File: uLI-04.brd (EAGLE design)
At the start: 57 x 38.5 mm, 39 parts, among them IC1 PIC18F14K50-I/SS, IC2 ADM2483, IC4 78L05F, J1 PICPROG2-V, J5 WEBP6-4, J6 WEBP6-4, J7 WEBP6-4, Q1 12.00 MHz, T1 IRF7306, X1 MINI-USB_SHIELD4P-USB-SPEC, X2 ARK1550/2_S

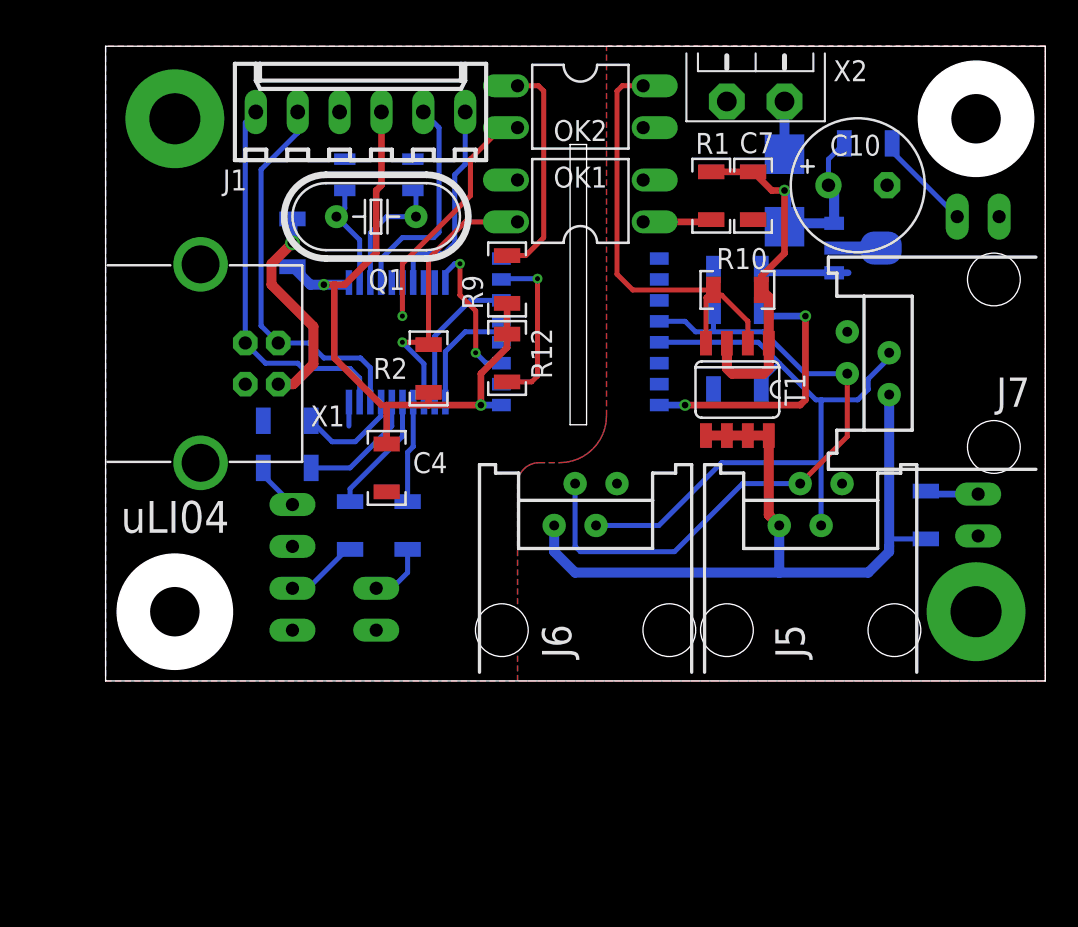
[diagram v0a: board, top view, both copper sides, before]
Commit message: uLI-04 rev 2.
Opraveny chyby uLI-04 zjistene behem testovani:
 * upraven obrys krabicky podle realnych rozmeru (zvetseno symtetricky 1 mm do sirky a 0.5 mm do vysky)
 * posunuty otvory pro srouby do krabicky o 0.5 mm v kazde ose smerrem ke kraji
 * prohozeno RX a TX mezi procesorem a ADUMem
 * opraveno zdcadlove zapojeni XpressNETich konektoru
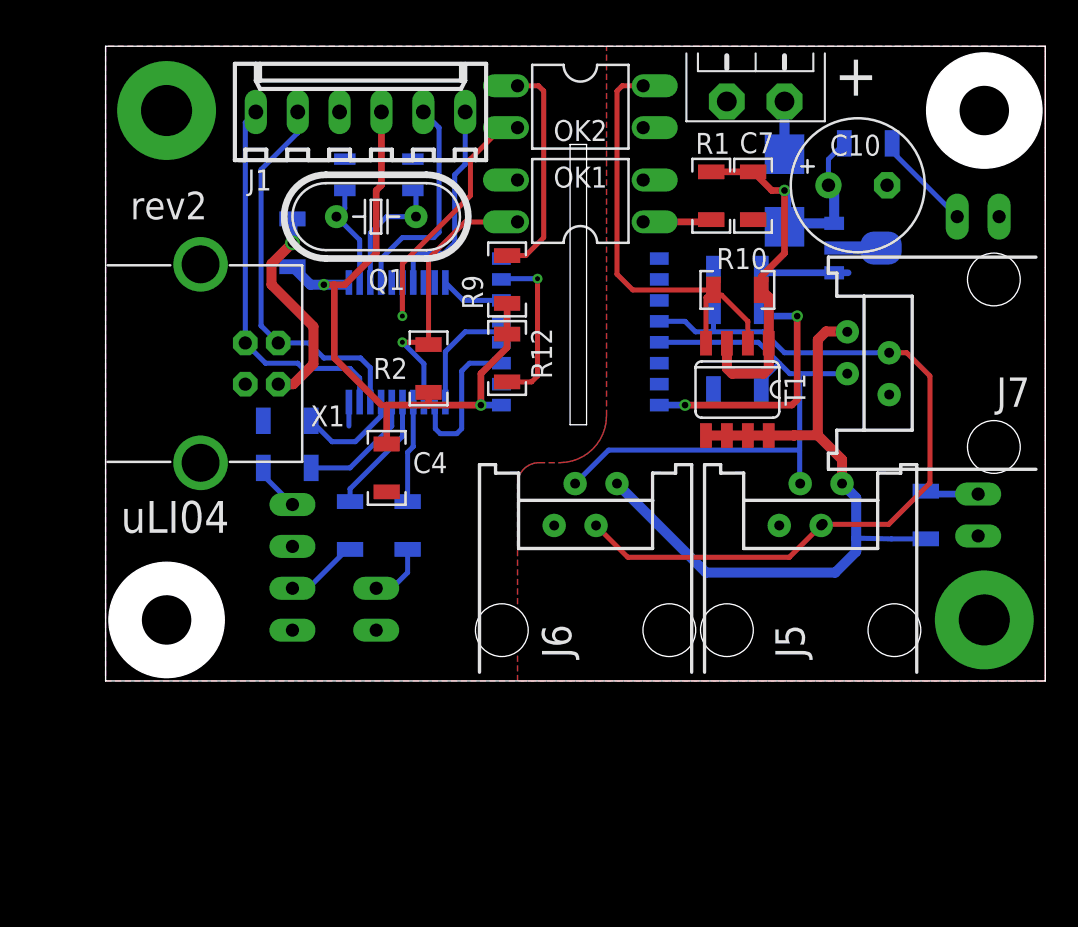
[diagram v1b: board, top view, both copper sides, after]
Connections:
- removed net PROC_TX: IC1.10, IC2.3
- new net N$5: IC1.12, IC2.3
- net +NAP: now also J5.4, J6.4, J7.4; no longer J5.1, J6.1, J7.1
- net BUS_A: now also J5.3, J6.3, J7.3; no longer J5.2, J6.2, J7.2
- net BUS_B: now also J5.2, J6.2, J7.2; no longer J5.3, J6.3, J7.3
- net GNDINT: now also J5.1, J6.1, J7.1; no longer J5.4, J6.4, J7.4
- net PROC_RX: now also IC1.10; no longer IC1.12
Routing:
- net N$5: track 0.00 -> 9.59 mm
- net PROC_TX: track 9.31 -> 0.00 mm, vias 2 -> 0
- net BUS_A: track 41.2 -> 48.7 mm, vias 0 -> 1
- net BUS_B: track 42.0 -> 35.4 mm
- net PROC_RX: track 8.94 -> 3.85 mm
- net +NAP: track 47.4 -> 44.1 mm
- net VCCINT: track 24.8 -> 23.8 mm
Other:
- outline, holes or cut-outs redrawn
- board text added: "+"
- board text added: "rev2"

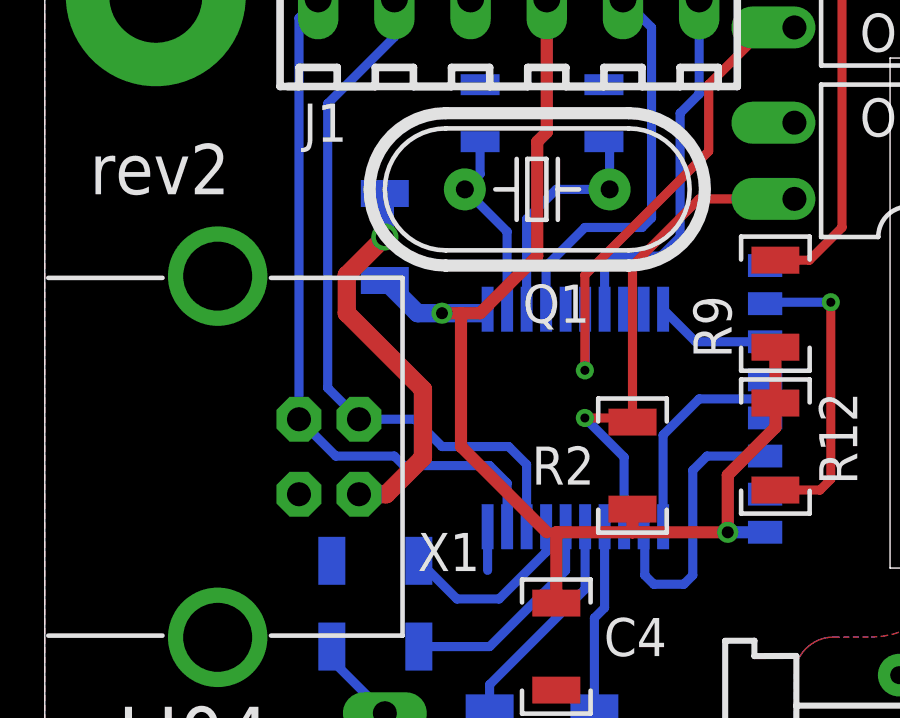
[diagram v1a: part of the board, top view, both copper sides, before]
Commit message: Odstranena ochrana dioda na vstupu z USB.
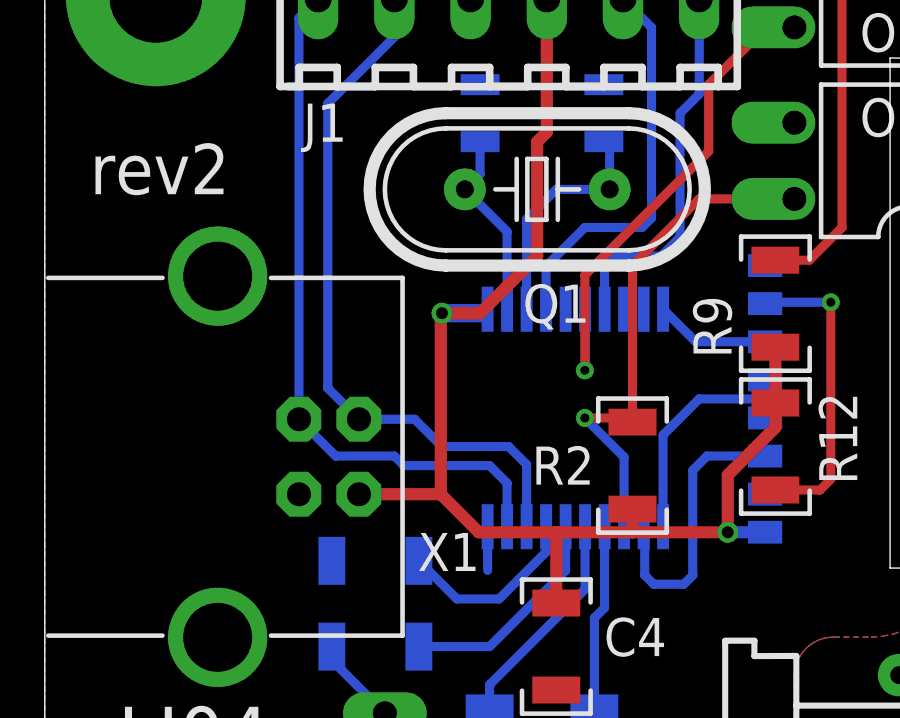
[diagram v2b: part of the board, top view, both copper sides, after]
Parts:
- removed D1: 1N4148-1206, diode:D1206
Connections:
- removed net N$10: D1.A, X1.1
- net VDD: now also X1.1; no longer D1.C
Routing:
- net N$10: track 13.0 -> 0.00 mm, vias 1 -> 0
- net VDD: track 42.3 -> 44.3 mm
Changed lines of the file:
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@@
 <layer number="14" name="Route14" color="1" fill="6" visible="no" active="no"/>
 <layer number="15" name="Route15" color="4" fill="6" visible="no" active="no"/>
-<layer number="16" name="Bottom" color="4" fill="1" visible="no" active="yes"/>
+<layer number="16" name="Bottom" color="4" fill="1" visible="yes" active="yes"/>
 <layer number="17" name="Pads" color="2" fill="1" visible="yes" active="yes"/>
 <layer number="18" name="Vias" color="2" fill="1" visible="yes" active="yes"/>
@@
 <layer number="20" name="Dimension" color="15" fill="1" visible="yes" active="yes"/>
 <layer number="21" name="tPlace" color="7" fill="1" visible="yes" active="yes"/>
-<layer number="22" name="bPlace" color="7" fill="1" visible="no" active="yes"/>
+<layer number="22" name="bPlace" color="7" fill="1" visible="yes" active="yes"/>
 <layer number="23" name="tOrigins" color="15" fill="1" visible="yes" active="yes"/>
-<layer number="24" name="bOrigins" color="15" fill="1" visible="no" active="yes"/>
-<layer number="25" name="tNames" color="7" fill="1" visible="yes" active="yes"/>
+<layer number="24" name="bOrigins" color="15" fill="1" visible="yes" active="yes"/>
+<layer number="25" name="tNames" color="7" fill="1" visible="no" active="yes"/>
 <layer number="26" name="bNames" color="7" fill="1" visible="no" active="yes"/>
 <layer number="27" name="tValues" color="7" fill="1" visible="no" active="yes"/>
@@
 <layer number="44" name="Drills" color="7" fill="1" visible="no" active="yes"/>
 <layer number="45" name="Holes" color="7" fill="1" visible="no" active="yes"/>
-<layer number="46" name="Milling" color="3" fill="1" visible="no" active="yes"/>
+<layer number="46" name="Milling" color="3" fill="1" visible="yes" active="yes"/>
 <layer number="47" name="Measures" color="7" fill="1" visible="no" active="yes"/>
 <layer number="48" name="Document" color="7" fill="1" visible="no" active="yes"/>
-<layer number="49" name="Reference" color="7" fill="1" visible="no" active="yes"/>
+<layer number="49" name="Reference" color="7" fill="1" visible="yes" active="yes"/>
 <layer number="50" name="dxf" color="7" fill="1" visible="no" active="no"/>
 <layer number="51" name="tDocu" color="7" fill="1" visible="yes" active="yes"/>
-<layer number="52" name="bDocu" color="7" fill="1" visible="no" active="yes"/>
+<layer number="52" name="bDocu" color="7" fill="1" visible="yes" active="yes"/>
 <layer number="53" name="tGND_GNDA" color="7" fill="9" visible="no" active="no"/>
 <layer number="54" name="bGND_GNDA" color="1" fill="9" visible="no" active="no"/>
@@
 <attribute name="VALUE" x="18.0975" y="31.4325" size="1.27" layer="28" ratio="15" rot="MR90"/>
 </element>
-<element name="D1" library="diode" package="D1206" value="1N4148-1206" x="13.335" y="28.575" smashed="yes" rot="MR270">
-<attribute name="NAME" x="14.2875" y="31.115" size="1.27" layer="26" ratio="15" rot="MR0"/>
-<attribute name="VALUE" x="11.875" y="34.345" size="1.27" layer="28" ratio="15" rot="MR270"/>
-</element>
 <element name="IC1" library="microchip" package="SSOP20" value="PIC18F14K50-I/SS" x="19.685" y="22.5425" smashed="yes" rot="MR180">
 <attribute name="NAME" x="15.6174" y="23.9385" size="1.27" layer="26" font="vector" ratio="15" rot="MR0"/>
@@
 <contactref element="IC1" pad="1"/>
 <contactref element="C4" pad="1"/>
-<contactref element="D1" pad="C"/>
 <contactref element="R2" pad="2"/>
 <via x="15.24" y="26.035" extent="1-16" drill="0.4"/>
@@
 <wire x1="18.415" y1="31.75" x2="18.415" y2="27.94" width="0.4064" layer="1"/>
 <wire x1="18.415" y1="27.94" x2="16.51" y2="26.035" width="0.4064" layer="1"/>
-<wire x1="16.51" y1="26.035" x2="15.875" y2="26.035" width="0.4064" layer="1"/>
-<wire x1="15.875" y1="26.035" x2="15.24" y2="26.035" width="0.4064" layer="1"/>
+<wire x1="16.51" y1="26.035" x2="15.24" y2="26.035" width="0.4064" layer="1"/>
 <wire x1="16.76" y1="26.1675" x2="16.6275" y2="26.035" width="0.3048" layer="16"/>
 <wire x1="16.6275" y1="26.035" x2="15.24" y2="26.035" width="0.6096" layer="16"/>
-<wire x1="18.7325" y1="18.7325" x2="15.875" y2="21.59" width="0.4064" layer="1"/>
-<wire x1="15.875" y1="21.59" x2="15.875" y2="26.035" width="0.4064" layer="1"/>
 <wire x1="26.0096" y1="18.7325" x2="24.765" y2="18.7325" width="0.4064" layer="16"/>
 <via x="24.765" y="18.7325" extent="1-16" drill="0.4"/>
 <wire x1="24.765" y1="18.7325" x2="21.59" y2="18.7325" width="0.4064" layer="1"/>
 <wire x1="21.59" y1="18.7325" x2="19.05" y2="18.7325" width="0.4064" layer="1"/>
-<wire x1="19.05" y1="18.7325" x2="18.7325" y2="18.7325" width="0.3048" layer="1"/>
 <wire x1="21.59" y1="19.505" x2="21.59" y2="18.7325" width="0.4064" layer="1"/>
-<wire x1="15.24" y1="26.035" x2="14.425" y2="26.035" width="0.6096" layer="16"/>
-<wire x1="13.335" y1="27.125" x2="14.425" y2="26.035" width="0.6096" layer="16"/>
 <wire x1="19.05" y1="16.3725" x2="19.05" y2="18.7325" width="0.4064" layer="1"/>
 <contactref element="J1" pad="3"/>
@@
 <wire x1="26.3525" y1="22.225" x2="26.3525" y2="23.04" width="0.4064" layer="1"/>
 <wire x1="26.3525" y1="23.04" x2="26.3525" y2="24.9025" width="0.4064" layer="1"/>
+<contactref element="X1" pad="1"/>
+<wire x1="19.05" y1="18.7325" x2="16.4675" y2="18.7325" width="0.4064" layer="1"/>
+<wire x1="12.4725" y1="20" x2="15.2" y2="20" width="0.4064" layer="1"/>
+<wire x1="15.2" y1="20" x2="15.2" y2="25.995" width="0.4064" layer="1"/>
+<wire x1="15.2" y1="25.995" x2="15.24" y2="26.035" width="0.4064" layer="1"/>
+<wire x1="16.4675" y1="18.7325" x2="15.2" y2="20" width="0.4064" layer="1"/>
 </signal>
 <signal name="PROC_RX">
@@
 <wire x1="45.847" y1="33.6445" x2="46.81" y2="34.6075" width="0.3048" layer="16"/>
 </signal>
-<signal name="N$10">
-<contactref element="X1" pad="1"/>
-<contactref element="D1" pad="A"/>
-<via x="13.335" y="28.575" extent="1-16" drill="0.6"/>
-<wire x1="13.335" y1="28.575" x2="12.065" y2="27.305" width="0.6096" layer="1"/>
-<wire x1="12.065" y1="27.305" x2="12.065" y2="26.035" width="0.6096" layer="1"/>
-<wire x1="12.065" y1="26.035" x2="14.605" y2="23.495" width="0.6096" layer="1"/>
-<wire x1="14.605" y1="23.495" x2="14.605" y2="21.22" width="0.6096" layer="1"/>
-<wire x1="13.335" y1="30.025" x2="13.335" y2="28.575" width="0.6096" layer="16"/>
-<wire x1="12.4725" y1="20" x2="13.385" y2="20" width="0.6096" layer="1"/>
-<wire x1="13.385" y1="20" x2="14.605" y2="21.22" width="0.6096" layer="1"/>
-</signal>
 <signal name="XTAL2">
